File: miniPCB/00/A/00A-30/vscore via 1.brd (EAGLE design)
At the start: 148.6 x 86.4 mm, 4 parts

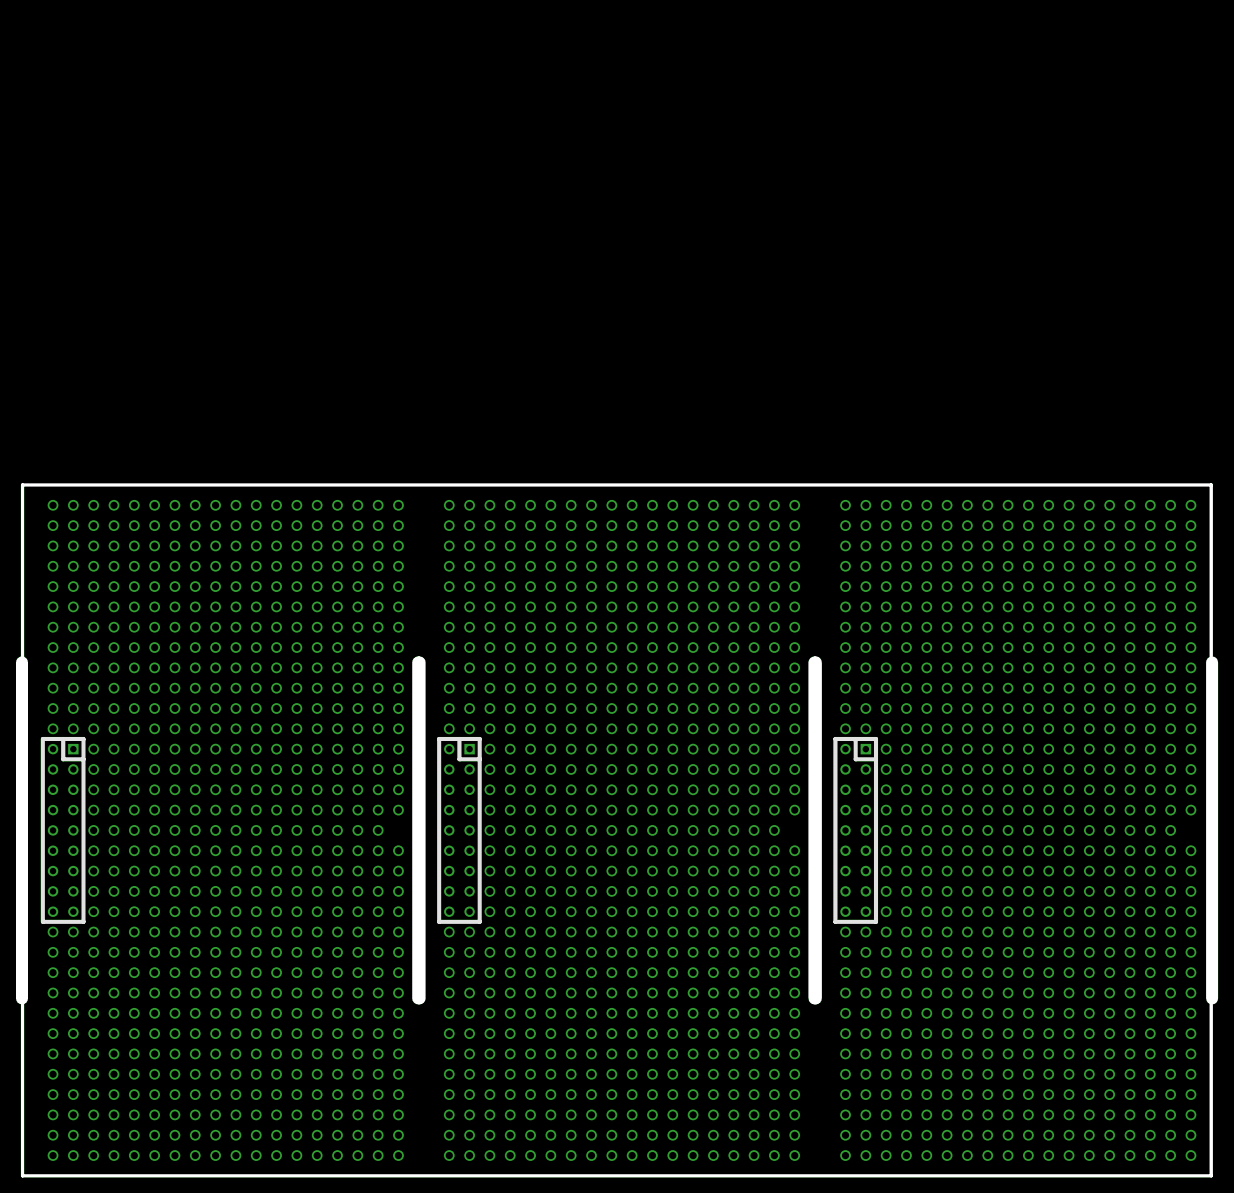
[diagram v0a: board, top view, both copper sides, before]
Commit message: Giving vScore boards regular part numbers
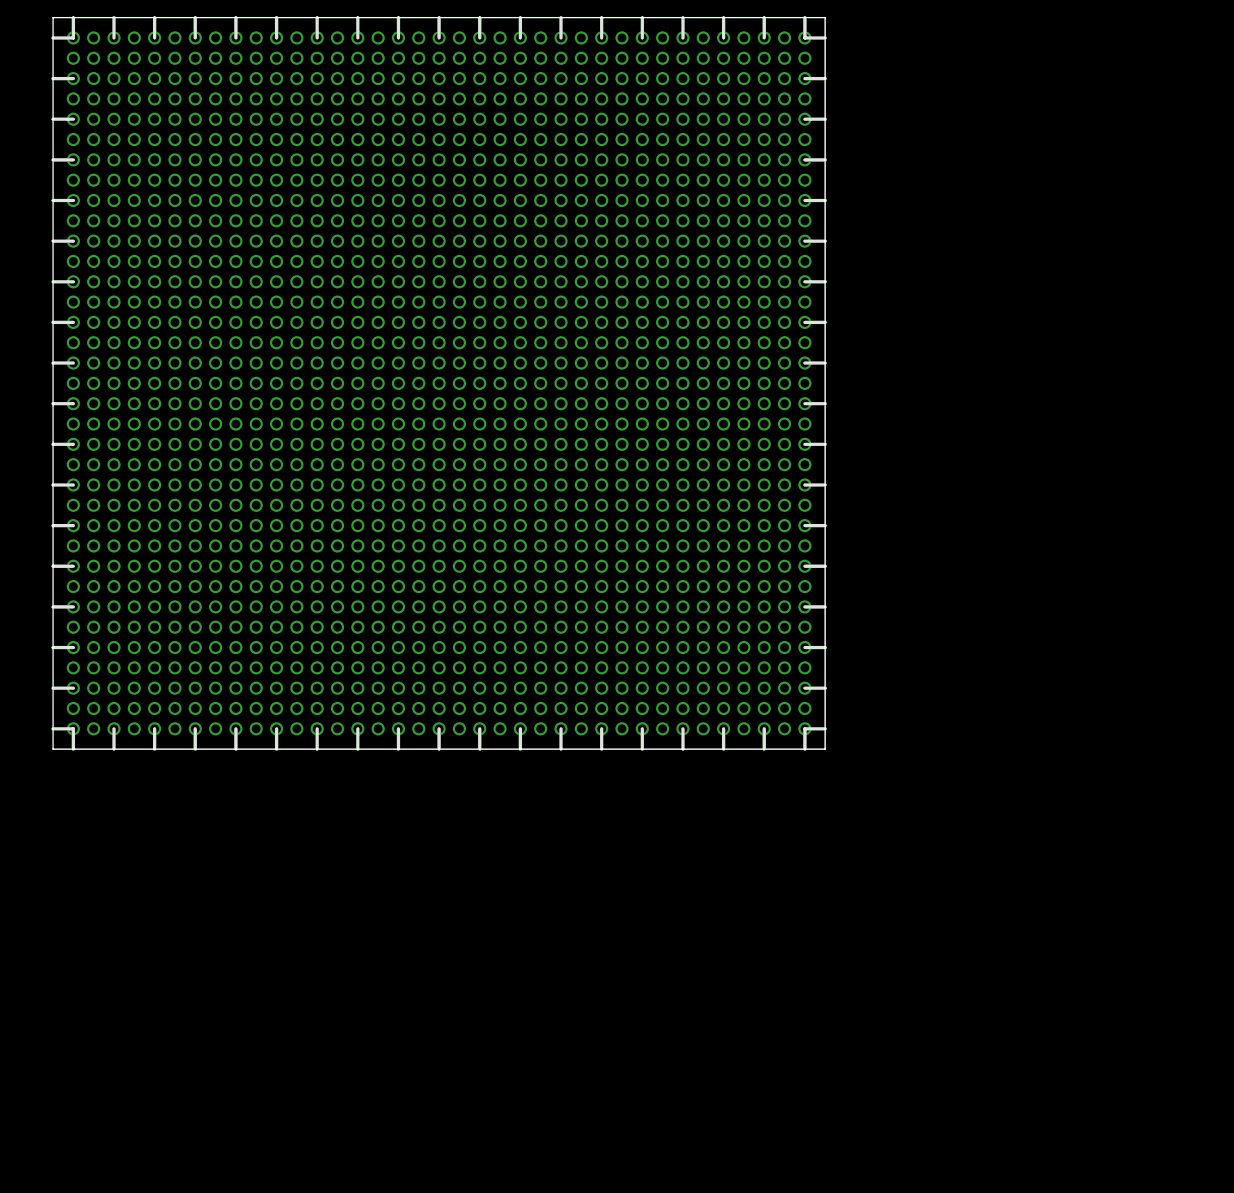
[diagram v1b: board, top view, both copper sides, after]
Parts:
- removed J1, J2, J3: (no value), miniPCB_BOARDS:BC_HOUSING_53MM
- moved E$1 56.8 mm to (-50.8, -63.5)
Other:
- board size 148.6 x 86.4 mm -> 96.5 x 91.4 mm
